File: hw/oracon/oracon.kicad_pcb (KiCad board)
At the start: 4 copper layers, 81 x 56 mm, 108 parts, among them J2 SIM_Card, J3 USB_A, J4 Conn_Coaxial, J5 USB_C_Receptacle_USB2.0_16P, Q1 SS8050, Q2 SS8050, Q3 SS8050, Q5 SS8050, SW1 SW_Push, U1 TP5100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

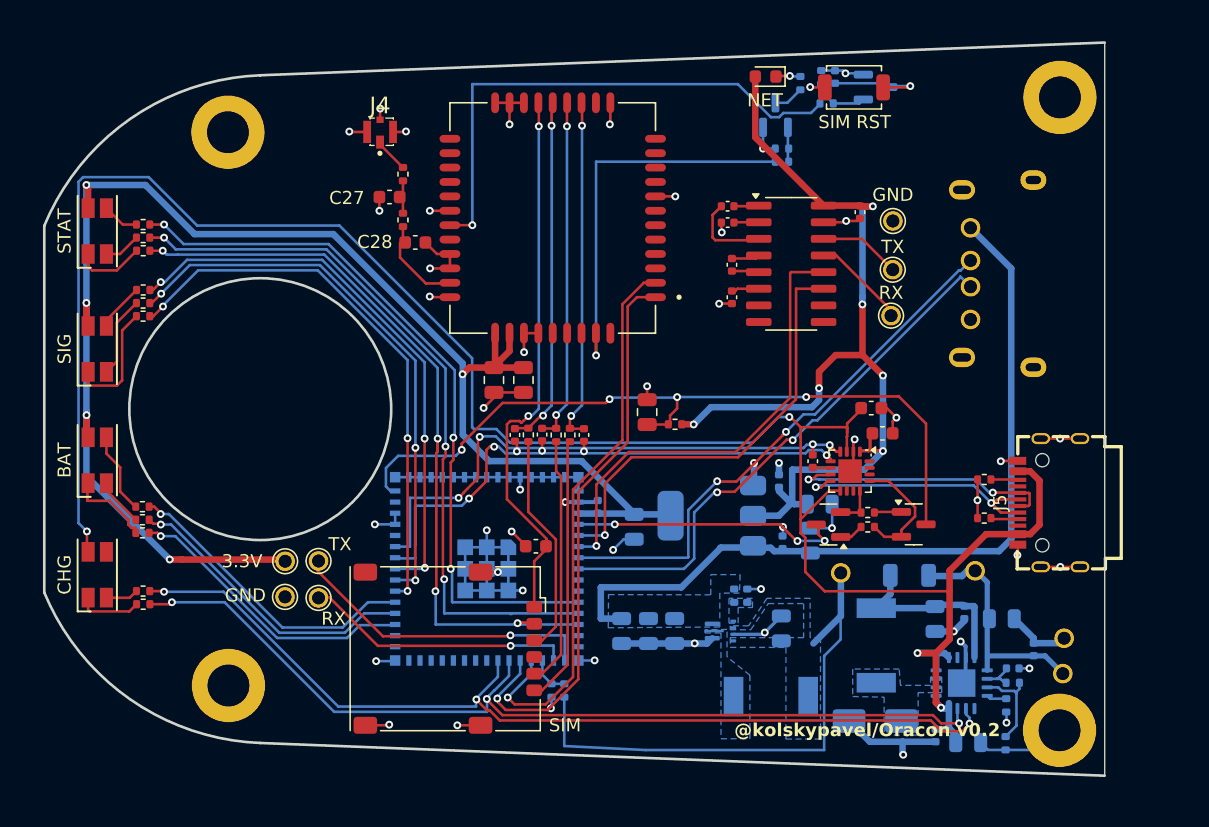
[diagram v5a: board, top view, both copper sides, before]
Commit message: fixed vias
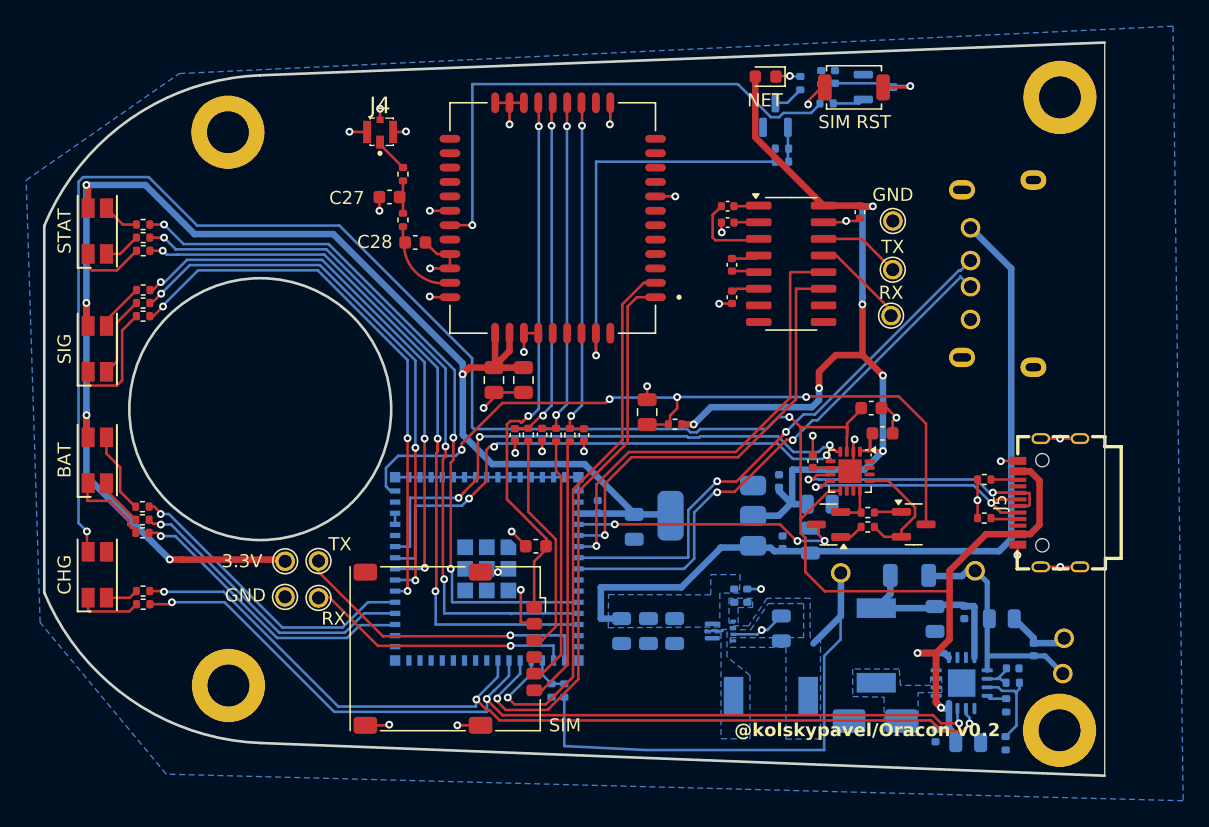
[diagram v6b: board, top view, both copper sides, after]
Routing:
- net GND: track 162.7 -> 91.3 mm, vias 56 -> 35
- net VBUS: track 166.1 -> 165.4 mm
- net RF_ANT: track 6.53 -> 5.98 mm
- added copper zone on B.Cu, net GND

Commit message: check
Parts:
- C27, C28: footprint Capacitor_SMD:C_0603_1608Metric -> Capacitor_SMD:C_0402_1005Metric
- moved C28 2.02 mm to (-9.98, 67.0), turned to 180 degrees
- moved J4 1.16 mm to (-9.50, 58.5)
- moved R32 1.04 mm to (-9.50, 62.5)
- moved R31 0.69 mm to (-9.50, 65.5)
- moved C27 0.60 mm to (-9.98, 64.0)
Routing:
- net GND: track 91.3 -> 88.3 mm, vias 35 -> 67
- net RF_ANT: track 5.98 -> 7.44 mm
- net +3.3V: track 189.3 -> 190.4 mm
- net Net-(C27-Pad1): track 2.48 -> 1.98 mm

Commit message: via stiching
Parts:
- moved C31 0.25 mm to (23.9, 54.3)
- moved R34 0.25 mm to (22.8, 54.3)
- moved R33 0.20 mm to (23.4, 56.0)
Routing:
- net GND: vias 67 -> 161
